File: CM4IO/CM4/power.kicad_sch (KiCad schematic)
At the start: 16 parts

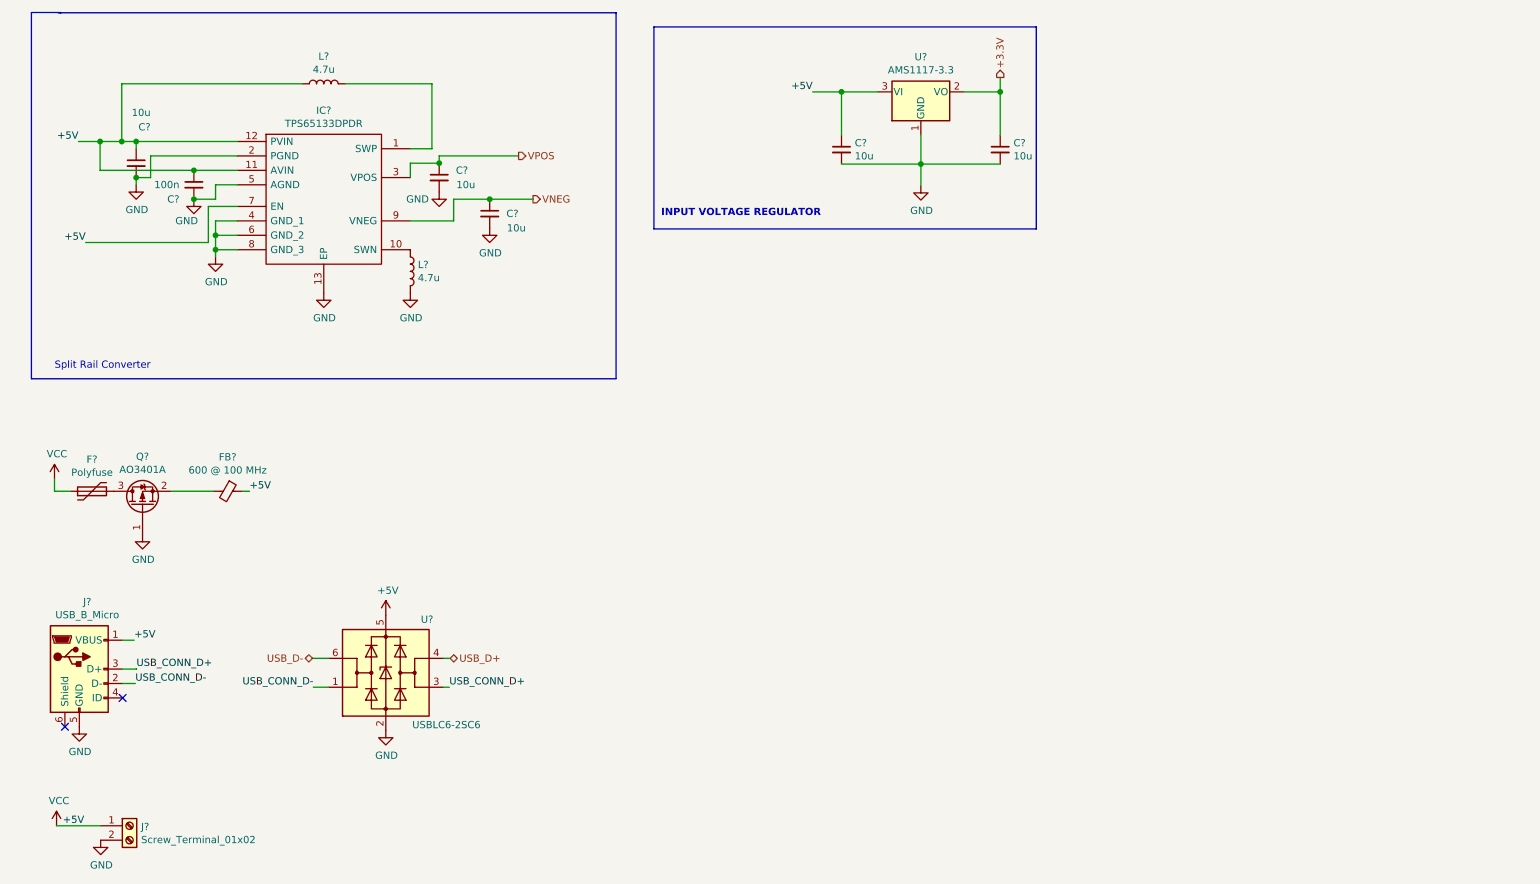
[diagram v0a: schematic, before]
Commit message: Initial CM4IO board design
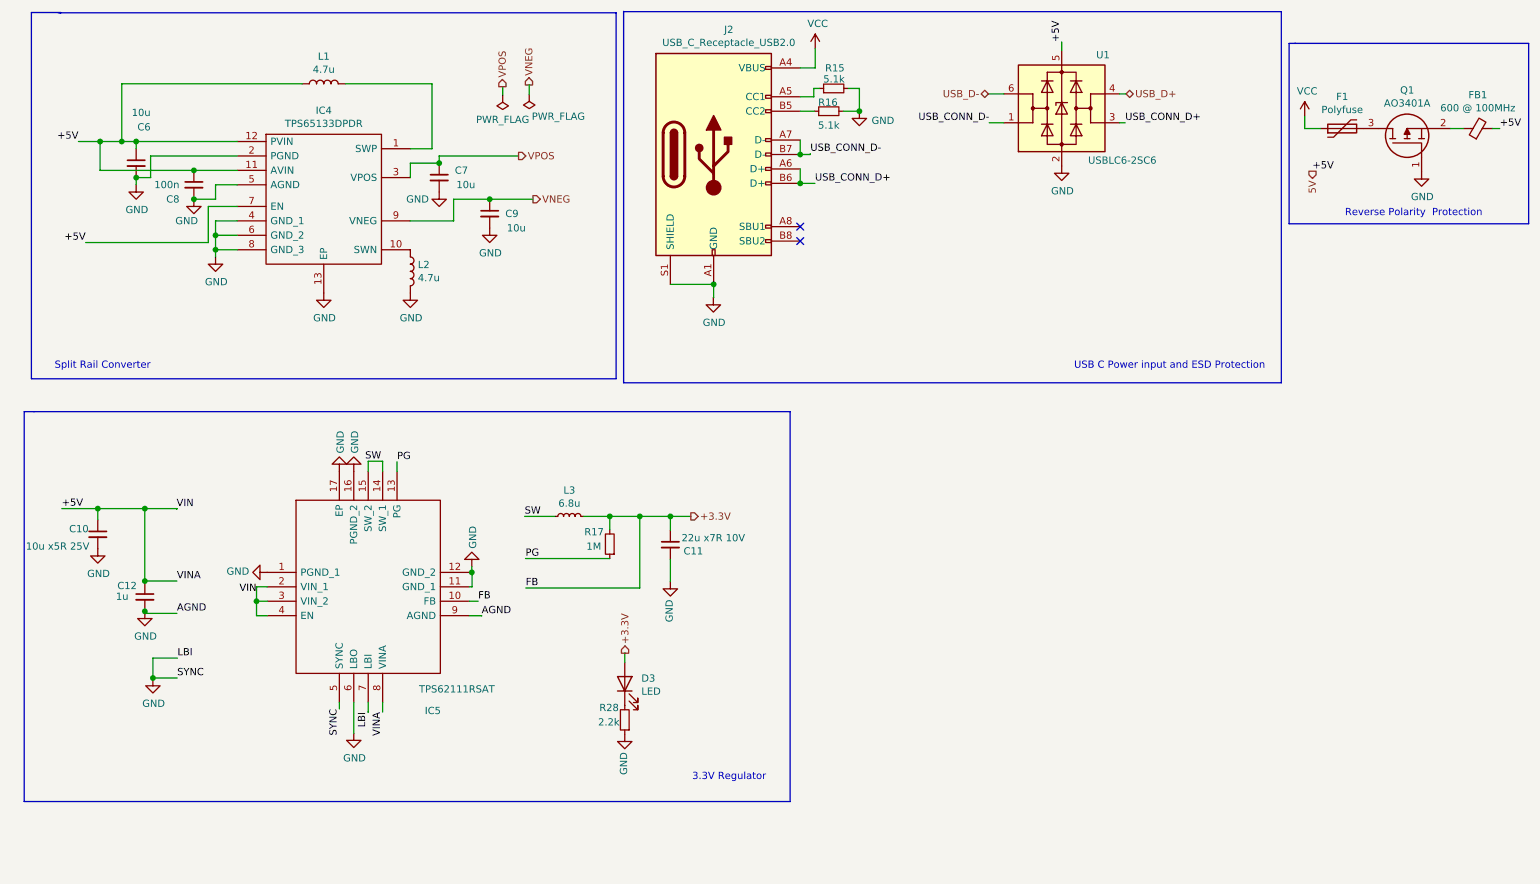
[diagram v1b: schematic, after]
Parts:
- removed C? (x2): 10u, Capacitor_SMD:C_0603_1608Metric, symbol Device:C_Small
- removed FB?: 600 @ 100 MHz, Inductor_SMD:L_0603_1608Metric, symbol F7_100pin-rescue:Ferrite_Bead_Small-Device
- removed J?: Screw_Terminal_01x02, symbol Connector:Screw_Terminal_01x02
- removed J?: USB_B_Micro, symbol Connector:USB_B_Micro
- removed Q?: AO3401A, Package_TO_SOT_SMD:SOT-23, symbol Transistor_FET:AO3401A
- removed U?: AMS1117-3.3, Package_TO_SOT_SMD:SOT-223-3_TabPin2, symbol Regulator_Linear:AMS1117-3.3
- added C10: 10u x5R 25V, Capacitor_SMD:C_1210_3225Metric, symbol Device:C_Small
- added C11: 22u x7R 10V, Capacitor_SMD:C_1210_3225Metric, symbol Device:C_Small
- added C12: 1u, Capacitor_SMD:C_0805_2012Metric, symbol Device:C_Small
- added D3: LED, LED_SMD:LED_0603_1608Metric, symbol Device:LED
- added FB1: 600 @ 100MHz, Inductor_SMD:L_0805_2012Metric, symbol Device:FerriteBead_Small
- added IC5: TPS62111RSAT, SamacSys_Parts:QFN65P400X400X100-17N-D, symbol SamacSys_Parts:TPS62111RSAT
- added J2: USB_C_Receptacle_USB2.0, CM4IO:TYPE-C-31-M-12, symbol Connector:USB_C_Receptacle_USB2.0
- added L3: 6.8u, Inductor_SMD:L_TDK_SLF7032, symbol Device:L_Small
- added Q1: AO3401A, SamacSys_Parts:SOT95P280X125-3N, symbol SamacSys_Parts:AO3401A
- added R15, R16: 5.1k, Resistor_SMD:R_1206_3216Metric, symbol Device:R_Small
- added R17: 1M, Resistor_SMD:R_0805_2012Metric, symbol Device:R_Small
- added R28: 2.2k, Resistor_SMD:R_0603_1608Metric, symbol Device:R_Small
- F1: renamed from F?; footprint (none) -> Fuse:Fuse_1206_3216Metric
- gave numbers to parts that had none: 8
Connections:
- net +3.3V: now also C11.1, D3.2 (A), IC5.10 (FB), L3.2, R17.2
- net GND: now also C10.2, C11.2, C12.2, IC5.1 (PGND_1), IC5.11 (GND_1), IC5.12 (GND_2), IC5.16 (PGND_2), IC5.17 (EP), IC5.5 (SYNC), IC5.6 (LBO), IC5.7 (LBI), IC5.9 (AGND), J2.A1 (GND), J2.A12 (GND), J2.B1 (GND), J2.B12 (GND), J2.S1 (SHIELD), Q1.1, R15.2, R16.2, R28.1
- net USB_CONN_D+: now also J2.A6 (D+), J2.B6 (D+)
- net USB_CONN_D-: now also J2.A7 (D-), J2.B7 (D-)
- net at F1.2: now also Q1.3
- net +5V renamed 5V
- net 5V: now also C10.1, C12.1, FB1.2, IC5.2 (VIN_1), IC5.3 (VIN_2), IC5.4 (EN), IC5.8 (VINA); no longer F1.1
- new net: J2.A5 (CC1), R15.1
- new net: J2.B5 (CC2), R16.1
- new net: FB1.1, Q1.2
- new net: D3.1 (K), R28.2
- new net PG: IC5.13 (PG), R17.1
- new net SW: IC5.14 (SW_1), IC5.15 (SW_2), L3.1
- new net VCC: F1.1, J2.A4 (VBUS), J2.A9 (VBUS), J2.B4 (VBUS), J2.B9 (VBUS)
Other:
- note added: "3.3V Regulator"
- note added: "Reverse Polarity Protection"
- note added: "USB C Power input and ESD Protection"
- note removed: "INPUT VOLTAGE REGULATOR"
- title: (none) -> USB Power and 3.3V
- moved on the sheet: F1, U1

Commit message: Completed H7/CM4IO Board
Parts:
- removed U1: USBLC6-2SC6, Package_TO_SOT_SMD:SOT-23-6, symbol Power_Protection:USBLC6-2SC6
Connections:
- net USB_CONN_D+: no longer names the net of J2.A6 (D+)
- net USB_CONN_D+: no longer J2.B6 (D+)
- net USB_CONN_D-: no longer names the net of J2.A7 (D-)
- net USB_CONN_D-: no longer J2.B7 (D-)
- no-connect marks 2 -> 6
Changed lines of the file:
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@@
   (junction (at 129.9972 102.8192) (diameter 1.016) (color 0 0 0 0))
   (junction (at 137.6172 61.976) (diameter 1.016) (color 0 0 0 0))
-  (junction (at 152.8572 39.116) (diameter 1.016) (color 0 0 0 0))
-  (junction (at 152.8572 44.196) (diameter 1.016) (color 0 0 0 0))
   (junction (at 163.2712 31.496) (diameter 1.016) (color 0 0 0 0))
   (no_connect (at 152.8572 54.356))
+  (no_connect (at 152.8572 36.576))
+  (no_connect (at 152.8572 41.656))
+  (no_connect (at 152.8572 39.116))
+  (no_connect (at 152.8572 44.196))
   (no_connect (at 152.8572 51.816))
   (wire (pts (xy 22.86 101.4476) (xy 29.21 101.4476))
@@
     (stroke (width 0) (type solid) (color 0 0 0 0))
   )
-  (wire (pts (xy 152.8572 36.576) (xy 152.8572 39.116))
-    (stroke (width 0) (type solid) (color 0 0 0 0))
-  )
-  (wire (pts (xy 152.8572 39.116) (xy 154.6352 39.116))
-    (stroke (width 0) (type solid) (color 0 0 0 0))
-  )
-  (wire (pts (xy 152.8572 41.656) (xy 152.8572 44.196))
-    (stroke (width 0) (type solid) (color 0 0 0 0))
-  )
-  (wire (pts (xy 152.8572 44.196) (xy 155.448 44.196))
-    (stroke (width 0) (type solid) (color 0 0 0 0))
-  )
-  (wire (pts (xy 154.6352 39.116) (xy 154.6352 38.9636))
-    (stroke (width 0) (type solid) (color 0 0 0 0))
-  )
   (wire (pts (xy 155.2448 27.4828) (xy 156.21 27.4828))
     (stroke (width 0) (type solid) (color 0 0 0 0))
@@
   )
   (wire (pts (xy 163.2712 27.4828) (xy 163.2712 31.496))
-    (stroke (width 0) (type solid) (color 0 0 0 0))
-  )
-  (wire (pts (xy 185.9788 28.448) (xy 188.722 28.448))
-    (stroke (width 0) (type solid) (color 0 0 0 0))
-  )
-  (wire (pts (xy 186.1312 33.528) (xy 188.722 33.528))
-    (stroke (width 0) (type solid) (color 0 0 0 0))
-  )
-  (wire (pts (xy 198.882 19.304) (xy 198.882 20.828))
-    (stroke (width 0) (type solid) (color 0 0 0 0))
-  )
-  (wire (pts (xy 209.042 28.448) (xy 210.2104 28.448))
-    (stroke (width 0) (type solid) (color 0 0 0 0))
-  )
-  (wire (pts (xy 209.042 33.528) (xy 210.058 33.528))
     (stroke (width 0) (type solid) (color 0 0 0 0))
   )
@@
     (effects (font (size 1.27 1.27)) (justify left bottom))
   )
-  (label "USB_CONN_D-" (at 154.6352 38.9636 0)
-    (effects (font (size 1.27 1.27)) (justify left bottom))
-  )
-  (label "USB_CONN_D+" (at 155.448 44.196 0)
-    (effects (font (size 1.27 1.27)) (justify left bottom))
-  )
-  (label "USB_CONN_D-" (at 186.1312 33.528 180)
-    (effects (font (size 1.27 1.27)) (justify right bottom))
-  )
-  (label "+5V" (at 198.882 19.304 90)
-    (effects (font (size 1.27 1.27)) (justify left bottom))
-  )
-  (label "USB_CONN_D+" (at 210.058 33.528 0)
-    (effects (font (size 1.27 1.27)) (justify left bottom))
-  )
   (label "+5V" (at 243.0272 42.0624 0)
     (effects (font (size 1.27 1.27)) (justify left bottom))
@@
   )
   (hierarchical_label "+3.3V" (shape output) (at 133.604 102.8192 0)
-    (effects (font (size 1.27 1.27)) (justify left))
-  )
-  (hierarchical_label "USB_D-" (shape bidirectional) (at 185.9788 28.448 180)
-    (effects (font (size 1.27 1.27)) (justify right))
-  )
-  (hierarchical_label "USB_D+" (shape bidirectional) (at 210.2104 28.448 0)
     (effects (font (size 1.27 1.27)) (justify left))
   )
@@
     )
     (property "Datasheet" "" (id 3) (at 163.2712 31.496 0)
-      (effects (font (size 1.27 1.27)) hide)
-    )
-  )
-  (symbol (lib_id "power:GND") (at 198.882 41.148 0) (unit 1)
-    (in_bom yes) (on_board yes)
-    (property "Reference" "#PWR04" (id 0) (at 198.882 47.498 0)
-      (effects (font (size 1.27 1.27)) hide)
-    )
-    (property "Value" "GND" (id 1) (at 199.009 45.5422 0))
-    (property "Footprint" "" (id 2) (at 198.882 41.148 0)
-      (effects (font (size 1.27 1.27)) hide)
-    )
-    (property "Datasheet" "" (id 3) (at 198.882 41.148 0)
       (effects (font (size 1.27 1.27)) hide)
     )
@@
     )
   )
-  (symbol (lib_id "Power_Protection:USBLC6-2SC6") (at 198.882 30.988 0) (unit 1)
-    (in_bom yes) (on_board yes)
-    (property "Reference" "U1" (id 0) (at 206.1464 21.5962 0))
-    (property "Value" "USBLC6-2SC6" (id 1) (at 209.55 40.1509 0))
-    (property "Footprint" "Package_TO_SOT_SMD:SOT-23-6" (id 2) (at 198.882 43.688 0)
-      (effects (font (size 1.27 1.27)) hide)
-    )
-    (property "Datasheet" "https://www.st.com/resource/en/datasheet/usblc6-2.pdf" (id 3) (at 203.962 22.098 0)
-      (effects (font (size 1.27 1.27)) hide)
-    )
-  )
